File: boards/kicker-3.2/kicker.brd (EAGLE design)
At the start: 141 x 146.1 mm, 151 parts, among them J1 B2PS-VH(LF)(SN), J2 HFW8R-1ST, J3 B2PS-VH(LF)(SN), J4 B2PS-VH(LF)(SN), J5 2-PIN_2MM-H, J6 3-PIN_2MM-H, J7 !BTN_KCK_PRE_EXT, J8 !BTN_CHP_PRE_EXT, J9 !BTN_CHG_PRE_EXT, Q1 ATP302ATPAK, Q10 BSS806NSOT-23-3, Q2 IRFS4227, Q3 BSS127, Q4 BSS127, Q5 BSS127, Q6 BSS127, Q7 AOD1N60, T1 DA203X-ALDA2034, U1 MPM3620GQV-P, U2 15V, U3 LT3751FE, U4 AT32ATQFP44, U5 IX4427N, U8 ADUM744XCRQZ-RL7, U9 ADUM744XARQZ-RL7

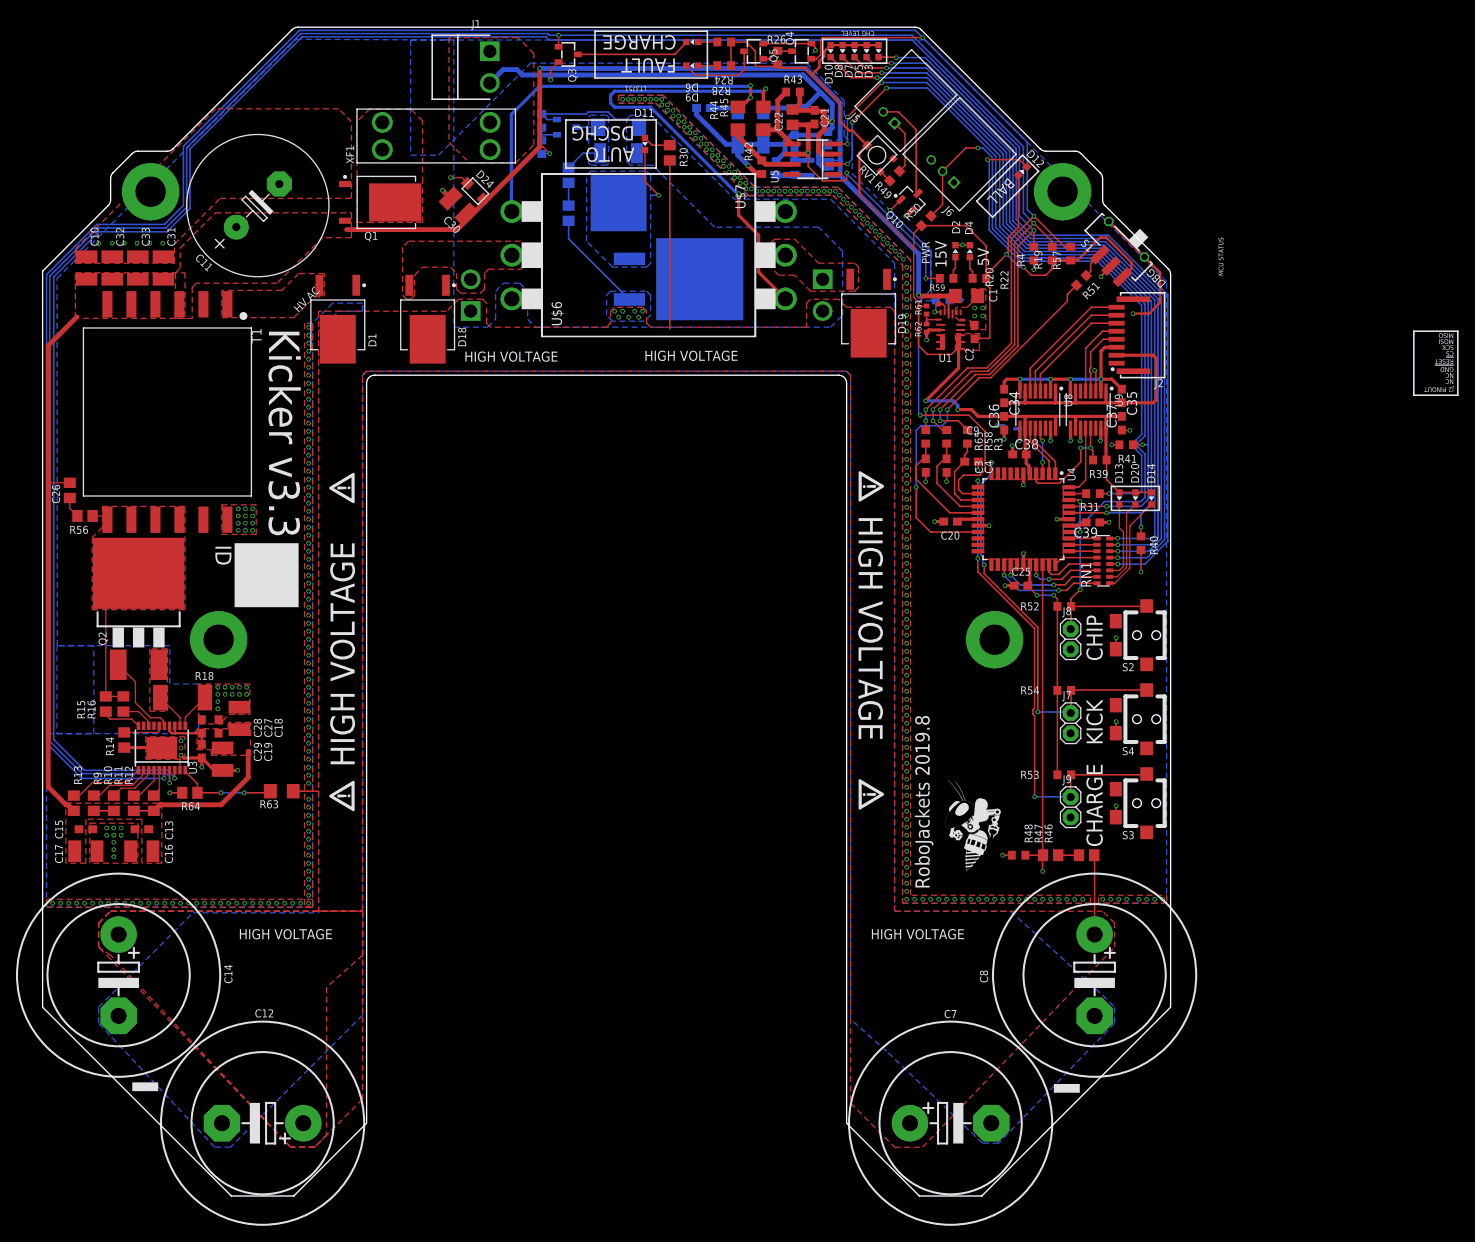
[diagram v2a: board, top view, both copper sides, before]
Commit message: updated LT calibration, added docs for LT
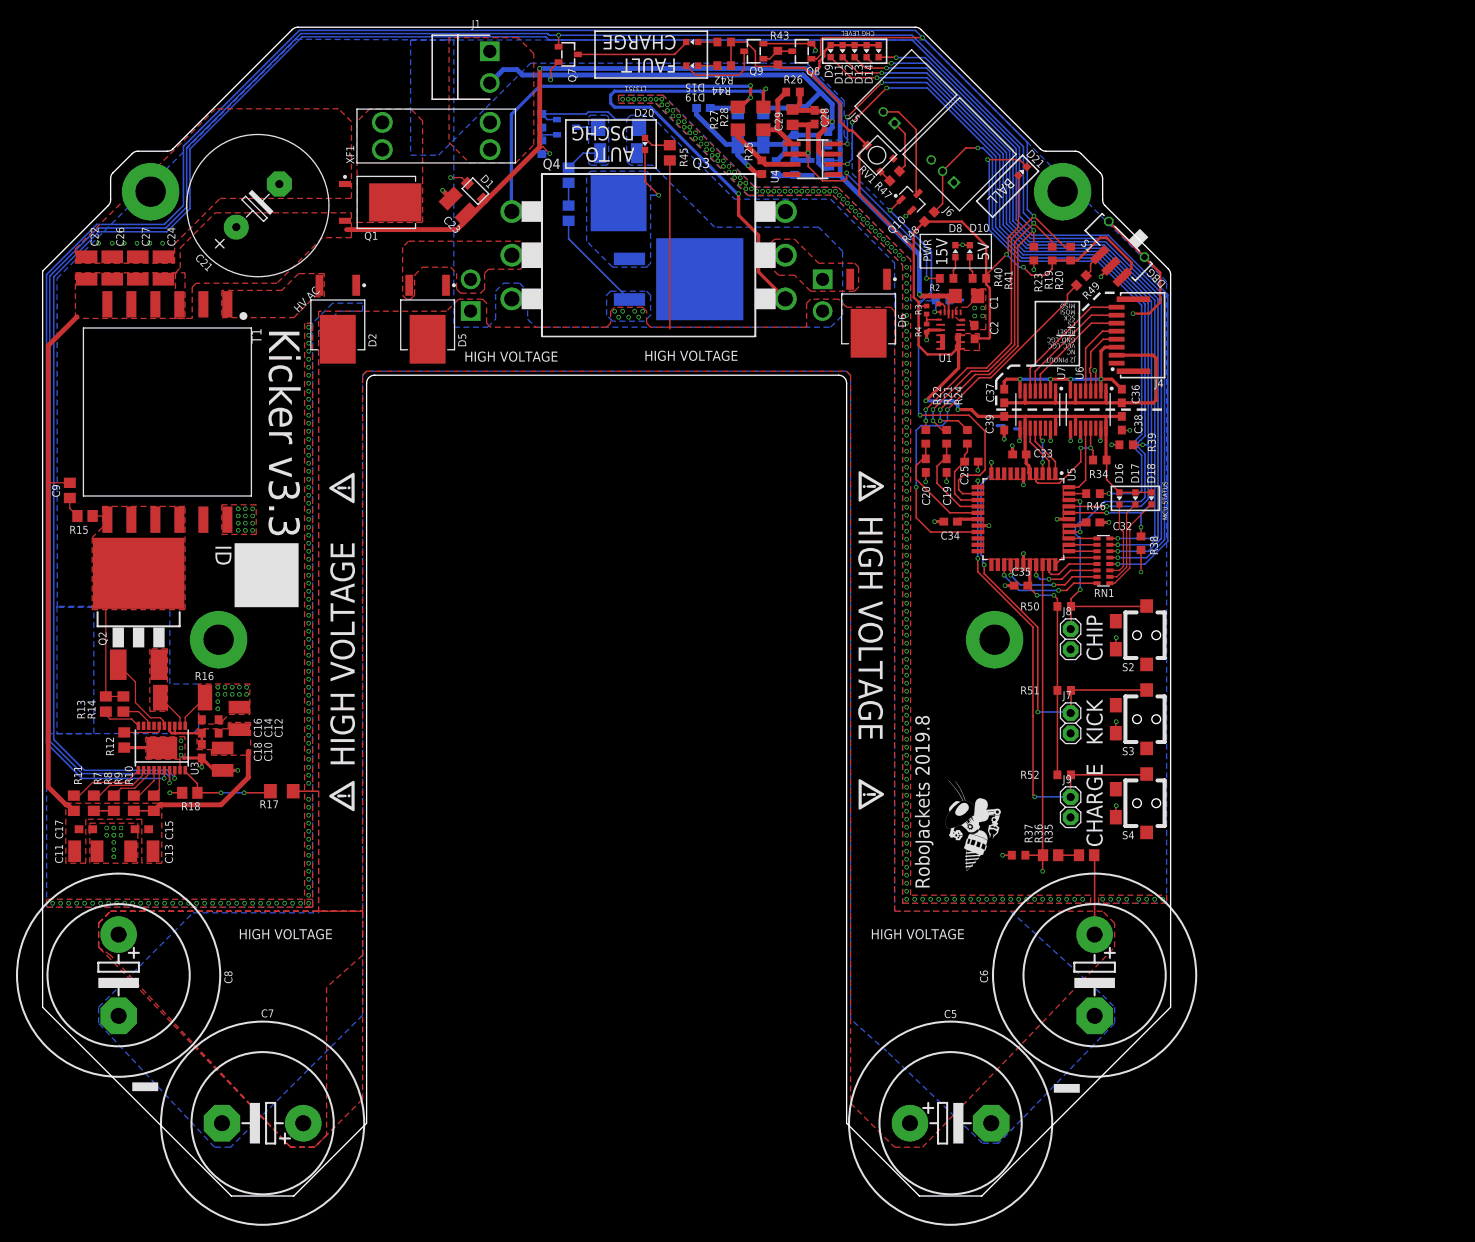
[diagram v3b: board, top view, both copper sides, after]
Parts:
- removed D24: PTVS20VS1UR, RoboJackets-Diodes:SOD123-W
- removed R53, R54: 10k, rcl:R0603
- removed R56: 22, resistor:R0805
- removed R57: 100k, rcl:R0603
- removed R59: 100k, rcl:R0402
- removed R60: 43.2k, rcl:R0603
- removed R61: 160k 1%, rcl:R0402
- removed R62: 30.1k 1%, rcl:R0402
- removed R64: 931, rcl:R0805
- removed R65: 160, rcl:R0603
- removed U$6, U$7: IXGK400N30A3, RoboJackets-Discrete:TO264
- added D21: BLUE, RoboJackets-LEDs:CHIP-LED0603
- added Q8, Q9: BSS127, RoboJackets-Discrete:SOT-23-3
- added R23: 100k, rcl:R0603
- added R25: 10k, rcl:R0603
- added R27: 160, rcl:R1206
- added R29: 270k, rcl:R0603
- added R32: ERJ-6GEYJ515V, rcl:R0805
- added R33: 1.5k 35W, RoboJackets-Resistors:TO508P1539X450-3
- added R5: 110k 1%, resistor:R0603
- added R6: 10k 1%, resistor:R0603
- added R7: 294k 1%, resistor:R0805
- added R8: 412k 1%, resistor:R0805
- C11: value 560uF -> 10uF (X7R); device rcl:E7,5-18 -> rcl:C1210
- C12: value 1000uF -> 10uF (X7R); device rcl:EB25D -> rcl:C1210
- C13, C27: value 0.1uF -> 10uF (X7R); device rcl:C0603 -> rcl:C1210
- C14: value 1000uF -> 0.1uF; device rcl:EB25D -> rcl:C0603
- C15: value 10pF -> 0.1uF; device resistor:C0603 -> rcl:C0603
- C16, C32, C33: value 10uF (X7R) -> 0.1uF; device rcl:C1210 -> rcl:C0603
- C17, C18: value 10uF (X7R) -> 10pF; device rcl:C1210 -> resistor:C0603
- C19: value 10uF (X7R) -> 1uF; device rcl:C1210 -> rcl:C0603
- C20, C25: value 0.1uF -> 1uF
- C21: value 0.1uF 35V -> 560uF; device rcl:C0603 -> rcl:E7,5-18
- C22: value 22uF 35V -> 10uF (X7R); device rcl:C0805 -> rcl:C1210
- C23, C24: value 0.1uF 50V -> 10uF (X7R); device rcl:C0603 -> rcl:C1210
- C26: value 220pF 100V -> 10uF (X7R); device resistor:C0805 -> rcl:C1210
- C28: value 0.1uF -> 0.1uF 35V
- C29: value 10pF -> 22uF 35V; device resistor:C0603 -> rcl:C0805
- C30, C31: value 10uF (X7R) -> 0.1uF 50V; device rcl:C1210 -> rcl:C0603
- C4: value 1uF -> 2.2uF
- C5: value 1uF -> 1000uF; device rcl:C0603 -> rcl:EB25D
- C6: value 2.2uF -> 1000uF; device rcl:C0603 -> rcl:EB25D
- C9: value 1uF -> 220pF 100V; device rcl:C0603 -> resistor:C0805
- D1: value VS-5EWH06FN-M3D-PAK_TO252AA -> PTVS20VS1UR; device RoboJackets-Diodes:TO460P990X239-3 -> RoboJackets-Diodes:SOD123-W
- D10, D8: value RED -> GREEN
- D11: value YELLOW -> RED
- D12: value BLUE -> YELLOW
- D13: value GREEN -> YELLOW
- D14: value RED -> BLUE
- D15: value 3SMBJ5929B-TP -> GREEN; device RoboJackets-Diodes:DO214AA -> RoboJackets-LEDs:CHIP-LED0603
- D16: value SMAJ20ADO-214AC -> GREEN; device RoboJackets-Diodes:RESM5226X262 -> RoboJackets-LEDs:CHIP-LED0603
- D17: value SMAJ20ADO-214AC -> YELLOW; device RoboJackets-Diodes:RESM5226X262 -> RoboJackets-LEDs:CHIP-LED0603
- D18, D19: value VS-5EWH06FN-M3D-PAK_TO252AA -> RED; device RoboJackets-Diodes:TO460P990X239-3 -> RoboJackets-LEDs:CHIP-LED0603
- D2, D6: value GREEN -> VS-5EWH06FN-M3D-PAK_TO252AA; device RoboJackets-LEDs:CHIP-LED0603 -> RoboJackets-Diodes:TO460P990X239-3
- D3: value BLUE -> SMAJ20ADO-214AC; device RoboJackets-LEDs:CHIP-LED0603 -> RoboJackets-Diodes:RESM5226X262
- D4: value GREEN -> SMAJ20ADO-214AC; device RoboJackets-LEDs:CHIP-LED0603 -> RoboJackets-Diodes:RESM5226X262
- D5: value YELLOW -> VS-5EWH06FN-M3D-PAK_TO252AA; device RoboJackets-LEDs:CHIP-LED0603 -> RoboJackets-Diodes:TO460P990X239-3
- D7: value YELLOW -> 3SMBJ5929B-TP; device RoboJackets-LEDs:CHIP-LED0603 -> RoboJackets-Diodes:DO214AA
- J2: value HFW8R-1ST -> B2PS-VH(LF)(SN); device RoboJackets-Connectors:HFW8R-1ST -> RoboJackets-Connectors:B2PS-CENTERED
- J4: value B2PS-VH(LF)(SN) -> HFW8R-1ST; device RoboJackets-Connectors:B2PS-CENTERED -> RoboJackets-Connectors:HFW8R-1ST
- Q3, Q4: value BSS127 -> IXGK400N30A3; device RoboJackets-Discrete:SOT-23-3 -> RoboJackets-Discrete:TO264
- Q6: value BSS127 -> AOD1N60; device RoboJackets-Discrete:SOT-23-3 -> RoboJackets-Discrete:DPAK
- Q7: value AOD1N60 -> BSS127; device RoboJackets-Discrete:DPAK -> RoboJackets-Discrete:SOT-23-3
- R1: value 110k 1% -> 43.2k; device resistor:R0603 -> rcl:R0603
- R11: value 294k 1% -> 25,5k 1%
- R12: value 412k 1% -> 1.00k 1%
- R13: value 40.2k 1% -> 11.5k 1%
- R14: value 1.62k 1% -> 25.5k 1%
- R15: value 18.2k 1% -> 22
- R16: value 40.2k 1% -> 15m 1%; device resistor:R0805 -> resistor:R2512
- R18: value 15m 1% -> 931; device resistor:R2512 -> rcl:R0805
- R2: value 10k 1% -> 100k; device resistor:R0603 -> rcl:R0402
- R20: value 1k -> 100k
- R22, R24: value 330 -> 160
- R26: value 1k -> 10k
- R28: value 330 -> 160; device rcl:R0603 -> rcl:R1206
- R3: value 160 -> 160k 1%; device rcl:R0603 -> rcl:R0402
- R30: value ERJ-P06J274V -> 100k; device rcl:R0805 -> rcl:R0603
- R31: value 60 -> ERJ-6GEYJ515V; device rcl:R0603 -> rcl:R0805
- R34: value 270k -> 10k
- R35: value 100k -> ERJ-6GEYJ515V; device rcl:R0603 -> rcl:R0805
- R37: value ERJ-6GEYJ515V -> RC0603FR-07205KL; device rcl:R0805 -> rcl:R0603
- R38: value 1.5k 35W -> 10k; device RoboJackets-Resistors:TO508P1539X450-3 -> rcl:R0603
- R4: value 100k -> 30.1k 1%; device rcl:R0603 -> rcl:R0402
- R40, R43: value 10k -> 1k
- R41, R42: value 10k -> 330
- R44: value 160 -> 330; device rcl:R1206 -> rcl:R0603
- R45: value 160 -> ERJ-P06J274V; device rcl:R1206 -> rcl:R0805
- R46: value ERJ-6GEYJ515V -> 60; device rcl:R0805 -> rcl:R0603
- R47: value ERJ-6GEYJ515V -> 50; device rcl:R0805 -> rcl:R0603
- R48: value RC0603FR-07205KL -> 10k
- R49: value 50 -> 10k
- U4: value AT32ATQFP44 -> IX4427N; device RoboJackets-ICs:QFP80P1200X1200X120-44 -> RoboJackets-PowerICs:SOIC-8
- U5: value IX4427N -> AT32ATQFP44; device RoboJackets-PowerICs:SOIC-8 -> RoboJackets-ICs:QFP80P1200X1200X120-44
- XF1: value 30A -> 20A
- moved C32 126.7 mm to (60.8, 15.6), turned to 180 degrees
- moved C5 124.0 mm to (43.0, -59.5), flipped to the top, turned to 0 degrees
- moved C8 122.0 mm to (-61.0, -41.0)
- moved R35 114.3 mm to (60.0, -26.0), flipped to the top, turned to 0 degrees
- moved C9 112.8 mm to (-67.1, 19.6), turned to 90 degrees
- moved C33 112.6 mm to (51.6, 24.1), turned to 0 degrees
- moved C6 110.7 mm to (61.0, -41.0), flipped to the top, turned to 270 degrees
- moved C29 108.3 mm to (23.2, 66.2)
- moved C28 108.0 mm to (26.0, 66.2), turned to 270 degrees
- moved R37 101.9 mm to (51.5, -26.0), flipped to the top, turned to 0 degrees
- moved R36 100.4 mm to (55.5, -26.0), flipped to the top, turned to 0 degrees
- moved C19 97.7 mm to (42.5, 22.7)
- moved D18 93.2 mm to (68.1, 18.6), turned to 180 degrees
- moved C22 90.2 mm to (-65.0, 47.4), turned to 90 degrees
- moved R47 87.1 mm to (36.0, 58.9), turned to 45 degrees
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- renumbered R58 to R21, R63 to R17, U8 to U7, U9 to U6
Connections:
- net !BTN_CHG: now also R52.1, S4.C, U5.12; no longer R53.1, S3.C, U4.12
- net !BTN_CHP: now also R50.1, U5.42; no longer R52.1, U4.42
- net !BTN_KCK: now also R51.1, S3.C, U5.11; no longer R54.1, S4.C, U4.11
- net !DONE!: now also C19.1, U5.15; no longer C4.1, U4.15
- net !DONE!_RAW: now also Q7.1; no longer Q3.1
- net !FAULT!: now also C20.1, R22.1, U5.16; no longer C3.1, R65.1, U4.16
- net !FAULT!_RAW: now also Q8.1, R20.1, R22.2; no longer Q4.1, R57.1, R65.2
- net !KICKER_SELECT: now also U5.44; no longer U4.44
- net !KICKER_SELECT_EXT: now also J4.5; no longer J2.5
- net !RESET: now also R34.1, U5.4; no longer R39.1, U4.4
- net !RESET_EXT: now also J4.4; no longer J2.4
- net +15.0V: now also C28.2, C29.2, C4.1, R40.2, R5.2, U4.6; no longer C21.2, C22.2, C6.1, R1.2, R20.2, U5.6
- net +5V: now also C32.2, C33.2, C34.2, C35.2, D11.A, D16.A, D17.A, D18.A, D21.A, D9.A, R20.2, R3.2, R34.2, R41.2, R42.2, R43.2, R44.2, R48.2, R51.2, U5.17, U5.27, U5.29, U5.38, U5.5; no longer C20.2, C25.2, C36.2, C37.2, D10.A, D20.A, D3.A, D5.A, D7.A, D8.A, R22.2, R24.2, R26.2, R28.2, R39.2, R53.2, R54.2, R57.2, R61.2, U4.17, U4.27, U4.29, U4.38, U4.5
- net 15V_PWR_BR: now also D8.A, R40.1; no longer D2.A, R20.1
- net BALL_SENSE: now also R46.2, U5.43; no longer R31.2, U4.43
- net BALL_SENSE_CL: now also D21.C, R46.1; no longer D12.C, R31.1
- net BB_RX: now also R48.1, U5.37; no longer R50.1, U4.37
- net BB_TX: now also U5.13; no longer U4.13
- net BB_TX_CL: now also R47.2; no longer R49.2
- net CHARGE: now also C25.1, R24.1, U5.14; no longer C9.1, R3.1, U4.14
- net CHARGE_RAW: now also R23.2, R24.2; no longer R3.2, R4.2
- net CHIP: now also R39.2, U4.2, U5.41; no longer R41.2, U4.41, U5.2
- net CHIPPER: now also D5.2, J2.2, Q3.C_BOT; no longer D18.2, J3.2, U$7.C_BOT
- net CHIP_GATE: now also R25.2, R27.1, U4.7; no longer R42.2, R44.1, U5.7
- net CHIP_GATE_S: now also C30.1, D3.2, Q3.G_BOT, R27.2; no longer C23.1, D16.2, R44.2, U$7.G_BOT
- net CSP: now also R16.2; no longer R18.2
- net DISCHARGE_DRAIN: now also D20.C, Q6.FIN, R33.2; no longer D11.C, Q7.FIN, R38.2
- net FAULT_INV_BR: now also Q8.3, Q9.1, R43.1; no longer Q4.3, Q5.1, R26.1
- net FB: now also R3.1, R4.2; no longer R61.1, R62.2
- net GND: now also C11.2, C12.2, C14.2, C20.2, C21.-, C22.2, C25.2, C26.2, C28.1, C29.1, C32.1, C33.1, C34.1, C35.1, C5.-, C6.-, D1.A, D10.C, D3.1, D4.1, D7.A, D8.C, Q3.E_BOT, Q4.E_BOT, Q6.3, Q7.2, Q8.2, Q9.2, R1.1, R12.2, R16.1, R18.2, R23.1, R25.1, R26.1, R30.1, R37.1, R38.1, R39.1, R6.1, U4.3, U5.18, U5.28, U5.39, U5.6; no longer C11.-, C12.-, C14.-, C20.1, C21.1, C22.1, C25.1, C28.2, C29.2, C32.2, C33.2, C36.1, C37.1, C5.2, C6.2, C9.2, D15.A, D16.1, D17.1, D2.C, D24.A, D4.C, Q3.2, Q4.2, Q6.2, Q7.3, R14.2, R18.1, R2.1, R35.1, R40.1, R41.1, R42.1, R43.1, R48.1, R60.1, R62.1, R64.2, U$6.E_BOT, U$7.E_BOT, U4.18, U4.28, U4.39, U4.6, U5.3
- net GND_LGC_EXT: now also C36.1, C37.1, J4.3; no longer C34.1, C35.1, J2.3
- net HV_AC: now also D2.2; no longer D1.2
- net HV_FB: now also R18.1; no longer R64.1
- net HV_IND_HIGH: now also U5.35; no longer U4.35
- net HV_IND_HIGH_CL: now also D11.C; no longer D8.C
- net HV_IND_LOW: now also U5.33; no longer U4.33
- net HV_IND_LOW_CL: now also D13.C; no longer D5.C
- net HV_IND_MAX: now also U5.36; no longer U4.36
- net HV_IND_MAX_CL: now also D9.C; no longer D10.C
- net HV_IND_MID: now also U5.34; no longer U4.34
- net HV_IND_MID_CL: now also D12.C; no longer D7.C
- net HV_IND_MIN: now also U5.32; no longer U4.32
- net HV_IND_MIN_CL: now also D14.C; no longer D3.C
- net HV_SENSE_DIV_BR: now also R35.1, R36.2; no longer R46.1, R47.2
- net KICK: now also R38.2, U4.4, U5.40; no longer R40.2, U4.40, U5.4
- net KICKER: now also D6.2, J3.1, Q4.C_BOT; no longer D19.2, J4.1, U$6.C_BOT
- net KICK_GATE: now also R26.2, R28.1, U4.5; no longer R43.2, R45.1, U5.5
- net KICK_GATE_S: now also C31.1, D4.2, Q4.G_BOT, R28.2; no longer C24.1, D17.2, R45.2, U$6.G_BOT
- net MCU_ERR: now also U5.25; no longer U4.25
- net MCU_ERR_CL: now also D18.C; no longer D14.C
- net MCU_INIT_OK: now also U5.30; no longer U4.30
- net MCU_INIT_OK_CL: now also D16.C; no longer D13.C
- net MCU_MODE: now also U5.26; no longer U4.26
- net MCU_MODE_CL: now also D17.C; no longer D20.C
- net MISO: now also U5.2; no longer U4.2
- net MISO_EXT: now also J4.8; no longer J2.8
- net MODE_SELECT: now also R49.2, U5.19; no longer R51.2, U4.19
- net MOSI: now also U5.1; no longer U4.1
- net MOSI_EXT: now also J4.7; no longer J2.7
- net N$1: now also R12.1; no longer R14.1
- net N$14: now also R49.1; no longer R51.1
- net N$16: now also R5.1, R6.2; no longer R1.1, R2.2
- net N$18: now also C9.1, R15.2; no longer C26.1, R56.2
- net N$20: now also D10.A, R41.1; no longer D4.A, R22.1
- net N$24: now also R11.1; no longer R13.1
- net N$27: now also D19.A, R44.1; no longer D9.A, R28.1
- net N$28: now also D19.C, Q9.3; no longer D9.C, Q5.3
- net N$29: now also D20.A, R45.1; no longer D11.A, R30.1
- net N$3: now also R47.1; no longer R49.1
- net N$37: now also D15.C, Q7.3; no longer D6.C, Q3.3
- net N$5: now also D15.A, R42.1; no longer D6.A, R24.1
- net OVLO1: now also R8.2; no longer R10.2
- net OVLO2: now also R10.2; no longer R12.2
- net QD_GATE_CTRL: now also Q5.1, R29.1, R30.2; no longer Q6.1, R34.1, R35.2
- net QD_PU_BR: now also R31.1, R32.2; no longer R36.1, R37.2
- net QUICK_DISCHARGE: now also D7.C, Q5.3, Q6.1, R32.1; no longer D15.C, Q6.3, Q7.1, R37.1
- net RDCM: now also R13.2; no longer R15.2
- net REG_AAM: now also R1.2; no longer R60.2
- net REG_EN: now also R2.2; no longer R59.2
- net RVOUT: now also R14.2; no longer R16.2
- net SCK: now also U5.3; no longer U4.3
- net SCK_EXT: now also J4.6; no longer J2.6
- net UVLO1: now also R7.2; no longer R9.2
- net UVLO2: now also R9.2; no longer R11.2
- net V+: now also C5.+, C6.+, D2.3, D5.3, D6.3, J2.1, J3.2, R31.2, R33.1, R35.2, R45.2; no longer C12.+, C14.+, D1.3, D18.3, D19.3, J3.1, J4.2, R30.2, R36.2, R38.1, R46.2
- net VBATT: now also C11.1, C12.1, C14.1, C21.+, C22.1, C23.1, C24.1, C26.1, C3.1, C9.2, D1.C, R11.2, R2.1, R29.2, R7.1, R8.1; no longer C11.+, C19.1, C26.2, C28.1, C29.1, C30.1, C31.1, C32.1, C33.1, C5.1, D24.C, R11.1, R12.1, R13.2, R34.2, R59.1
- net VCC_LGC_EXT: now also C36.2, C37.2, J4.2; no longer C34.2, C35.2, J2.2
- net VMON: now also R36.1, R37.2, U5.31; no longer R47.1, R48.2, U4.31
- net VSN: now also R13.1, R14.1; no longer R16.1, R56.1
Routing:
- net BB_RX: track 82.7 -> 82.0 mm
- net GND: vias 373 -> 372
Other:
- board text added: "GND_LGC"
- board text added: "VCC_LGC"
- board text removed: "GND"

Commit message: kicker dr fixes
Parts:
- removed C17, C18: 10pF, resistor:C0603
- C10, C11, C12, C13: value 10uF (X7R) -> 10uF (X7R) 35V
- C14, C15, C16: value 0.1uF -> 0.1uF 35V
- C3: value 1uF -> 1uF 50V
- C4: value 2.2uF -> 2.2uF 35V
- D2, D5, D6: value VS-5EWH06FN-M3D-PAK_TO252AA -> VS-5EWH06FN-M3
- D3, D4: value SMAJ20ADO-214AC -> SMAJ20A
- R1: value 43.2k -> 43.2k 1%
- R11: value 25,5k 1% -> 25.5k 1%
- R16: value 15m 1% -> 15m 1% >0.5W
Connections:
- net GND: no longer C17.2, C18.2
- net VBATT: no longer C17.1, C18.1
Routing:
- net GND: track 214.7 -> 209.1 mm, vias 372 -> 371
- net VBATT: track 218.4 -> 217.0 mm

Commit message: passing core fixes
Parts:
- R2, R3, R4: device rcl:R0402 -> rcl:R0603
- R47: value 50 -> 51
- U6: value ADUM744XARQZ-RL7 -> ADUM7441ARQZ-RL7
- U7: value ADUM744XCRQZ-RL7 -> ADUM7441CRQZ-RL7
- moved C25 3.00 mm to (45.6, 26.2)
- moved R24 3.00 mm to (45.1, 23.3)
- moved R2 1.91 mm to (41.3, 45.3)
- moved R40 1.80 mm to (44.3, 46.1), flipped to the bottom, turned to 0 degrees
- moved R4 1.12 mm to (39.8, 38.8)
- moved R3 0.22 mm to (39.8, 42.0)
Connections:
- removed net N$2: U7.3
- net CHARGE: no longer C25.1
- net CHARGE_RAW: now also C25.1
- net GND: now also U7.3
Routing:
- net CHARGE_RAW: track 266.0 -> 269.0 mm
- net CHARGE: track 10.2 -> 7.81 mm
- net REG_EN: track 1.65 -> 2.99 mm
- net VBATT: track 217.0 -> 215.7 mm
- net +5V: track 231.6 -> 232.7 mm
- net 15V_PWR_BR: track 2.75 -> 3.49 mm, vias 0 -> 1
- net FB: track 2.82 -> 3.40 mm
- net +15.0V: track 40.0 -> 40.4 mm, vias 3 -> 2
- net GND: track 209.1 -> 208.8 mm, vias 371 -> 372

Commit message: final fixes and docs
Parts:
- removed C38, C39: 0.1uF, rcl:C0603
- added C17, C18: 1uF, rcl:C0603
- added R53: 10k, rcl:R0603
- C19: value 1uF -> 560uF; device rcl:C0603 -> rcl:E7,5-18
- C20, C25: value 1uF -> 10uF (X7R); device rcl:C0603 -> rcl:C1210
- C21: value 560uF -> 10uF (X7R); device rcl:E7,5-18 -> rcl:C1210
- C22: value 10uF (X7R) -> 1uF; device rcl:C1210 -> rcl:C0603
- C26: value 10uF (X7R) -> 0.1uF 35V; device rcl:C1210 -> rcl:C0603
- C27: value 10uF (X7R) -> 22uF 35V; device rcl:C1210 -> rcl:C0805
- C28: value 0.1uF 35V -> 0.1uF 50V
- C29: value 22uF 35V -> 0.1uF 50V; device rcl:C0805 -> rcl:C0603
- C30, C31: value 0.1uF 50V -> 0.1uF
- R17: value 187k -> 505k 0.1%; device rcl:R1206 -> rcl:R0603
- R18: value 931 -> 113k 0.1%; device rcl:R0805 -> rcl:R0603
- R19: value 100k -> 3.0k 0.1%
- R21, R24: value 160 -> 100k
- R23: value 100k -> 160
- R25: value 10k -> 160
- R27: value 160 -> 10k; device rcl:R1206 -> rcl:R0603
- R29: value 270k -> 160; device rcl:R0603 -> rcl:R1206
- R30: value 100k -> 270k
- R31: value ERJ-6GEYJ515V -> 100k; device rcl:R0805 -> rcl:R0603
- R33: value 1.5k 35W -> ERJ-6GEYJ515V; device RoboJackets-Resistors:TO508P1539X450-3 -> rcl:R0805
- R34: value 10k -> 1.5k 35W; device rcl:R0603 -> RoboJackets-Resistors:TO508P1539X450-3
- R35: value ERJ-6GEYJ515V -> 10k; device rcl:R0805 -> rcl:R0603
- R37: value RC0603FR-07205KL -> ERJ-6GEYJ515V; device rcl:R0603 -> rcl:R0805
- R38: value 10k -> RC0603FR-07205KL
- R40: value 1k -> 10k
- R41, R44: value 330 -> 1k
- R43: value 1k -> 330
- R45: value ERJ-P06J274V -> 330; device rcl:R0805 -> rcl:R0603
- R46: value 60 -> ERJ-P06J274V; device rcl:R0603 -> rcl:R0805
- R47: value 51 -> 60
- R48: value 10k -> 51
- moved R19 127.1 mm to (-52.1, -18.2), turned to 180 degrees
- moved C22 112.6 mm to (45.6, 26.2), turned to 0 degrees
- moved C20 107.8 mm to (-65.0, 47.4), turned to 90 degrees
- moved C25 106.3 mm to (-58.6, 47.4), turned to 90 degrees
- moved C19 92.0 mm to (-43.6, 55.2), turned to 45 degrees
- moved C26 89.8 mm to (26.0, 66.2), turned to 270 degrees
- moved C27 84.0 mm to (23.2, 66.2), turned to 270 degrees
- moved C30 71.1 mm to (60.8, 15.6), flipped to the top, turned to 180 degrees
- moved R46 67.9 mm to (7.90, 61.8), turned to 270 degrees
- moved R34 57.3 mm to (9.00, 46.0), flipped to the bottom, turned to 180 degrees
- moved C31 51.4 mm to (51.6, 24.1), flipped to the top, turned to 0 degrees
- moved R35 49.4 mm to (61.6, 23.4)
- moved R47 46.8 mm to (60.8, 19.2), turned to 180 degrees
- moved R25 44.8 mm to (45.1, 23.3)
- moved R42 43.5 mm to (46.6, 46.1)
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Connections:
- new net N$2: R17.2, R18.1
- net !BTN_CHG: now also R53.1; no longer R52.1
- net !BTN_CHP: now also R51.1; no longer R50.1
- net !BTN_KCK: now also R52.1; no longer R51.1
- net !DONE!: now also C17.1, R22.1; no longer C19.1, R21.1
- net !DONE!_RAW: now also R20.1, R22.2; no longer R19.1, R21.2
- net !FAULT!: now also C18.1, R23.1; no longer C20.1, R22.1
- net !FAULT!_RAW: now also R21.1, R23.2; no longer R20.1, R22.2
- net !RESET: now also R35.1; no longer R34.1
- net +15.0V: now also C26.2, C27.2, R41.2; no longer C28.2, C29.2, R40.2
- net +5V: now also C30.2, C31.2, C36.2, C37.2, R21.2, R35.2, R45.2, R49.2, R53.2; no longer C34.2, C35.2, C38.2, C39.2, R19.2, R34.2, R41.2, R48.2, R50.2
- net 15V_PWR_BR: now also R41.1; no longer R40.1
- net BALL_SENSE: now also R47.2; no longer R46.2
- net BALL_SENSE_CL: now also R47.1; no longer R46.1
- net BB_RX: now also R49.1; no longer R48.1
- net BB_TX_CL: now also R48.2; no longer R47.2
- net CHARGE: now also R25.1; no longer R24.1
- net CHARGE_RAW: now also C22.1, R25.2; no longer C25.1, R23.2
- net CHIP: now also R40.2; no longer R39.2
- net CHIP_GATE: now also R26.2, R28.1; no longer R25.2, R27.1
- net CHIP_GATE_S: now also C28.1, R28.2; no longer C30.1, R27.2
- net DISCHARGE_DRAIN: now also R34.2; no longer R33.2
- net FAULT_INV_BR: now also R44.1; no longer R43.1
- net GND: now also C17.2, C18.2, C19.-, C21.2, C26.1, C27.1, C28.2, C29.2, C30.1, C31.1, C36.1, C37.1, R19.2, R24.1, R27.1, R31.1, R40.1; no longer C19.2, C21.-, C26.2, C27.2, C28.1, C29.1, C30.2, C31.2, C34.1, C35.1, C38.1, C39.1, R18.2, R23.1, R25.1, R30.1, R37.1
- net GND_LGC_EXT: now also C34.1, C35.1; no longer C36.1, C37.1
- net HV_FB: now also R18.2, R19.1; no longer R17.2, R18.1
- net HV_SENSE_DIV_BR: now also R36.1, R37.2; no longer R35.1, R36.2
- net KICK: now also R39.2; no longer R38.2
- net KICK_GATE: now also R27.2, R29.1; no longer R26.2, R28.1
- net KICK_GATE_S: now also C29.1, R29.2; no longer C31.1, R28.2
- net MODE_SELECT: now also R50.2; no longer R49.2
- net N$14: now also R50.1; no longer R49.1
- net N$20: now also R42.1; no longer R41.1
- net N$27: now also R45.1; no longer R44.1
- net N$29: now also R46.1; no longer R45.1
- net N$3: now also R48.1; no longer R47.1
- net N$5: now also R43.1; no longer R42.1
- net QD_GATE_CTRL: now also R30.1, R31.2; no longer R29.1, R30.2
- net QD_PU_BR: now also R32.1, R33.2; no longer R31.1, R32.2
- net QUICK_DISCHARGE: now also R33.1; no longer R32.1
- net V+: now also R32.2, R34.1, R36.2, R46.2; no longer R31.2, R33.1, R35.2, R45.2
- net VBATT: now also C19.+, C20.1, C21.1, C25.1, R30.2; no longer C21.+, C22.1, C26.1, C27.1, R29.2
- net VCC_LGC_EXT: now also C34.2, C35.2; no longer C36.2, C37.2
- net VMON: now also R37.1, R38.2; no longer R36.1, R37.2
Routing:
- net HV_FB: track 12.7 -> 11.0 mm
- net N$2: track 0.00 -> 1.60 mm
